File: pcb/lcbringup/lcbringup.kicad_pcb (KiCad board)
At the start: 4 copper layers, 198 parts, among them J1 XILINX_JTAG, J10 SMPM, J11 ARF6-08-S-D-A-K-TR, J12 SMPM, J13 SMPM, J14 SMPM, J15 SMPM, J16 SMPM, J17 SMPM, J18 SMPM, J19 SMPM, J2 CONN_01X10, J20 SMPM, J21 SMPM, J22 SMPM, J3 CONN_SFP_HOST, J4 CORTEX_DEBUG_ETM, J5 CONN_01X03, J6 CONN_01X03, J7 SFP_CAGE, J8 CONN_IBC_MGMT, J9 CONN_ATX12V, M1 SCREWHOLE, M2 SCREWHOLE, M3 SCREWHOLE, M4 SCREWHOLE, U1 XC7A35T-2FGG484C, U10 MUN12AD03-SE, U11 MUN12AD03-SE, U2 STM32H735-UFBGA176-25, U3 ECS-1612MV-250-CN, U4 ECS-1612MV-250-CN, U5 MUN12AD03-SE, U6 ECS-1612MV-250-CN, U7 AT24MAC402, U8 SIT9121AI-2BF-XXS156.250000G, U9 MUN12AD03-SE

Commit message: Continued lcbringup layout
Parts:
- removed D6, D7, D8, D9: GREEN, azonenberg_pcb:EIA_0402_LED
- removed J6: CONN_01X03, azonenberg_pcb:CONN_HEADER_2.54MM_1x3
- removed R12, R13, R14, R15: 33K, azonenberg_pcb:EIA_0402_RES_NOSILK
- removed R25: 33, azonenberg_pcb:EIA_0402_RES_NOSILK
- removed U6: ECS-1612MV-250-CN, azonenberg_pcb:OSCILLATOR_1.6x1.2
- added C92: 0.47 uF, azonenberg_pcb:EIA_0402_CAP_NOSILK, F.Cu at (92.5, 118.0)
- added J23: CONN_IBC_MGMT_HOST, azonenberg_pcb:CONN_MOLEX_PICOBLADE_5POS_0532610571, F.Cu at (62.8, 112.0)
- C14, C15, C17, C18, C19, C2, C21, C22, C23, C24, C25, C26, C27, C28, C29, C33, C34, C35, C36, C42, C44, C47, C48, C49, C51, C52, C54, C55, C56, C57, C58, C59, C69, C7, C70, C71, C78, C8, C9, R11, R2, R24, R3, R34, R4, U8: moved to B.Cu
- C61: value 0.47 uF -> 4.7 uF; footprint azonenberg_pcb:EIA_0402_CAP_NOSILK -> azonenberg_pcb:EIA_0603_CAP_NOSILK
- moved J10 137.6 mm to (12.6, 29.2)
- moved J11 137.6 mm to (32.6, 30.3)
- moved J12 137.6 mm to (18.1, 29.2)
- moved J13 137.6 mm to (23.6, 29.2)
- moved J14 137.6 mm to (12.6, 35.9)
- moved J15 137.6 mm to (18.1, 35.9)
- moved J16 137.6 mm to (23.6, 35.9)
- moved J17 137.6 mm to (12.6, 42.5)
- moved J18 137.6 mm to (18.1, 42.5)
- moved J19 137.6 mm to (23.6, 42.5)
- moved J20 137.6 mm to (12.6, 49.1)
- moved J21 137.6 mm to (18.1, 49.1)
- moved J22 137.6 mm to (23.6, 49.1)
- moved C72 110.5 mm to (-3.78, 69.4)
- moved C73 110.5 mm to (-3.78, 70.9)
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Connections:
- net /MCU/SUPER_I2C_SCL renamed /Power supply/SUPER_I2C_SCL
- net /MCU/SUPER_I2C_SDA renamed /Power supply/SUPER_I2C_SDA
- C70 pad 2: /SFP/GTP_REF_P -> /SFP/GTP_REF_N
- C71 pad 2: /SFP/GTP_REF_N -> /SFP/GTP_REF_P
- J3 pad 12: /SFP/SFP_RX_P -> /SFP/SFP_RX_N
- J3 pad 13: /SFP/SFP_RX_N -> /SFP/SFP_RX_P
- R24 pad 2: Net-(J6-P2) -> /GND
- U1 pad A18: unconnected-(U1F-IO_L17P_T2_16-PadA18) -> /MCU/FMC_AD8
- U1 pad A19: unconnected-(U1F-IO_L17N_T2_16-PadA19) -> /MCU/FMC_AD11
- U1 pad A20: unconnected-(U1F-IO_L16N_T2_16-PadA20) -> /MCU/FMC_AD15
- U1 pad A21: unconnected-(U1F-IO_L21N_T3_DQS_16-PadA21) -> /MCU/FMC_AD14
- U1 pad B18: unconnected-(U1F-IO_L11N_T1_SRCC_16-PadB18) -> /MCU/FMC_AD12
- U1 pad B20: unconnected-(U1F-IO_L16P_T2_16-PadB20) -> /MCU/FMC_AD13
- U1 pad B21: unconnected-(U1F-IO_L21P_T3_DQS_16-PadB21) -> /MCU/FMC_AD10
- U1 pad B22: unconnected-(U1F-IO_L20N_T3_16-PadB22) -> /MCU/FMC_A17
- U1 pad C22: unconnected-(U1F-IO_L20P_T3_16-PadC22) -> /MCU/FMC_A16
- U1 pad D21: unconnected-(U1F-IO_L23N_T3_16-PadD21) -> /MCU/FMC_A18
- U1 pad D22: unconnected-(U1F-IO_L22N_T3_16-PadD22) -> /MCU/FMC_AD0
- U1 pad E21: unconnected-(U1F-IO_L23P_T3_16-PadE21) -> /MCU/FMC_NE3
- U1 pad E22: unconnected-(U1F-IO_L22P_T3_16-PadE22) -> /MCU/FMC_NE1
- U1 pad G13: /MCU/FMC_AD13 -> unconnected-(U1E-IO_L1N_T0_AD0N_15-PadG13)
- U1 pad G15: /MCU/FMC_AD12 -> unconnected-(U1E-IO_L2P_T0_AD8P_15-PadG15)
- U1 pad G16: /MCU/FMC_AD10 -> unconnected-(U1E-IO_L2N_T0_AD8N_15-PadG16)
- U1 pad G18: /MCU/FMC_AD8 -> unconnected-(U1E-IO_L4N_T0_AD9N_15-PadG18)
- U1 pad G20: /MCU/FMC_NE1 -> /MCU/FMC_NWAIT
- U1 pad H13: /MCU/FMC_AD11 -> unconnected-(U1E-IO_L1P_T0_AD0P_15-PadH13)
- U1 pad H19: /MCU/FMC_AD15 -> /MCU/FMC_AD2
- U1 pad H20: /MCU/FMC_NWE -> /MCU/FMC_AD3
- U1 pad H22: /MCU/FMC_NE3 -> /MCU/FMC_NWE
- U1 pad J14: /MCU/FMC_AD9 -> /MCU/FMC_AD1
- U1 pad J16: /MCU/FMC_A18 -> unconnected-(U1E-IO_0_15-PadJ16)
- U1 pad J17: /MCU/FMC_A19 -> unconnected-(U1E-IO_L21N_T3_DQS_A18_15-PadJ17)
- U1 pad J20: /MCU/FMC_A24 -> /MCU/FMC_NOE
- U1 pad J21: /MCU/FMC_NL_NADV -> /MCU/FMC_NE2
- U1 pad J22: /MCU/FMC_AD0 -> /MCU/FMC_A25
- U1 pad K13: /MCU/FMC_A17 -> unconnected-(U1E-IO_L19P_T3_A22_15-PadK13)
- U1 pad K14: /MCU/FMC_AD14 -> unconnected-(U1E-IO_L19N_T3_A21_VREF_15-PadK14)
- U1 pad K16: /MCU/FMC_A21 -> unconnected-(U1E-IO_L23N_T3_FWE_B_15-PadK16)
- U1 pad K17: /MCU/FMC_NOE -> unconnected-(U1E-IO_L21P_T3_DQS_15-PadK17)
- U1 pad K18: /MCU/FPGA_CLK_25MHZ -> unconnected-(U1E-IO_L13P_T2_MRCC_15-PadK18)
- U1 pad K19: /MCU/FPGA_LED_0 -> /MCU/FMC_NBL1
- U1 pad K21: /MCU/FMC_AD2 -> /MCU/FMC_A24
- U1 pad K22: /MCU/FMC_NWAIT -> /MCU/FMC_NL_NADV
- U1 pad L13: /MCU/FMC_A23 -> unconnected-(U1E-IO_L20N_T3_A19_15-PadL13)
- U1 pad L15: /MCU/FMC_AD1 -> unconnected-(U1E-IO_L22N_T3_A16_15-PadL15)
- U1 pad L16: /MCU/FMC_A20 -> unconnected-(U1E-IO_L23P_T3_FOE_B_15-PadL16)
- U1 pad L18: /MCU/FMC_A22 -> unconnected-(U1E-IO_L16N_T2_A27_15-PadL18)
- U1 pad L19: /MCU/FPGA_LED_3 -> /MCU/FMC_A22
- U1 pad L20: unconnected-(U1E-IO_L14N_T2_SRCC_15-PadL20) -> /MCU/FMC_AD9
- U1 pad L21: /MCU/FMC_AD3 -> /MCU/FMC_NBL0
- U1 pad M13: /MCU/FMC_NBL0 -> unconnected-(U1E-IO_L20P_T3_A20_15-PadM13)
- U1 pad M17: /MCU/FPGA_LED_2 -> unconnected-(U1E-IO_25_15-PadM17)
- U1 pad M18: /MCU/FMC_A25 -> unconnected-(U1E-IO_L16P_T2_A28_15-PadM18)
- U1 pad M21: /MCU/FMC_NE2 -> /MCU/FMC_A23
- U1 pad M22: unconnected-(U1E-IO_L15N_T2_DQS_ADV_B_15-PadM22) -> /MCU/FMC_A19
- U1 pad N18: /MCU/FMC_NBL1 -> unconnected-(U1E-IO_L17P_T2_A26_15-PadN18)
- U1 pad N19: /MCU/FMC_A16 -> unconnected-(U1E-IO_L17N_T2_A25_15-PadN19)
- U1 pad N20: unconnected-(U1E-IO_L18P_T2_A24_15-PadN20) -> /MCU/FMC_A21
- U1 pad N22: /MCU/FPGA_LED_1 -> /MCU/FMC_A20
- U2 pad M1: unconnected-(U2C-PC2-PadM1) -> /MCU/MCU_LED_0
- U2 pad M2: unconnected-(U2C-PC3-PadM2) -> /MCU/MCU_LED_1
- U2 pad N11: /MCU/MCU_LED_1 -> unconnected-(U2F-PF13-PadN11)
- U2 pad N13: /MCU/MCU_LED_0 -> unconnected-(U2H-PH8-PadN13)
- U2 pad N7: /MCU/MCU_LED_3 -> unconnected-(U2F-PF11-PadN7)
- U2 pad P1: unconnected-(U2A-PA0-PadP1) -> /MCU/MCU_LED_2
- U2 pad P11: /MCU/MCU_LED_2 -> unconnected-(U2F-PF12-PadP11)
- U2 pad P2: unconnected-(U2A-PA1-PadP2) -> /MCU/MCU_LED_3
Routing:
- net /GND: track 0.00 -> 665.9 mm, vias 0 -> 179
- net /3V3: track 0.00 -> 252.0 mm, vias 0 -> 63
- net /SFP/SFP_I2C_SDA: track 0.00 -> 71.6 mm, vias 0 -> 6
- net /SFP/SFP_I2C_SCL: track 0.00 -> 66.2 mm, vias 0 -> 4
- net /1V0: track 0.00 -> 56.3 mm, vias 0 -> 22
- net /MCU/MCU_UART_RX: track 0.00 -> 36.9 mm, vias 0 -> 1
- net /MCU/FMC_AD9: track 0.00 -> 36.3 mm, vias 0 -> 4
- net /MCU/MCU_UART_TX: track 0.00 -> 36.1 mm, vias 0 -> 1
- net /MCU/FMC_AD8: track 0.00 -> 34.8 mm
- net /MCU/VSMPS: track 0.00 -> 31.6 mm, vias 0 -> 7
- net /MCU/FMC_AD12: track 0.00 -> 31.2 mm
- net /SFP/SFP_RX_P: track 0.00 -> 30.8 mm
- net /SFP/SFP_RX_N: track 0.00 -> 30.8 mm
- net /MCU/FMC_AD11: track 0.00 -> 29.9 mm
- net /MCU/FMC_AD6: track 0.00 -> 28.6 mm, vias 0 -> 1
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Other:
- board outline added: 80.8 x 80.5 mm
- board text added: "GND"
- board text added: "LED0"
- board text added: "LED1"
- board text added: "LED2"
- board text added: "LED3"
- board text added: "RX"
- board text added: "TX"
- board text added: "VDDA"

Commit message: Continued line card bringup board
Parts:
- C38, C62, C63, C67, C68, C92, R22, R23, R26, R27, R28, TP2, U7: moved to B.Cu
- C40: value 2.2 uF -> 4.7 uF; footprint azonenberg_pcb:EIA_0805_CAP_NOSILK -> azonenberg_pcb:EIA_0603_CAP_NOSILK; moved to B.Cu
- C44: value 2.2 uF -> 4.7 uF; footprint azonenberg_pcb:EIA_0805_CAP_NOSILK -> azonenberg_pcb:EIA_0603_CAP_NOSILK
- moved R28 103.0 mm to (97.0, 40.0)
- moved R23 102.2 mm to (97.0, 41.5)
- moved R22 80.6 mm to (79.0, 60.5), turned to -90 degrees
- moved TP2 68.1 mm to (111.0, 57.5), turned to 180 degrees
- moved C40 64.8 mm to (112.5, 61.0), turned to 90 degrees
- moved U7 57.3 mm to (124.5, 61.8)
- moved C63 57.0 mm to (85.0, 58.5), turned to -90 degrees
- moved C62 56.5 mm to (89.5, 57.0)
- moved C92 55.6 mm to (88.0, 62.5), turned to 90 degrees
- moved C67 55.3 mm to (86.0, 61.5), turned to -90 degrees
- moved C38 55.2 mm to (102.5, 68.8), turned to 180 degrees
- moved C68 51.8 mm to (123.0, 63.2), turned to 90 degrees
- moved TP1 50.3 mm to (120.0, 79.5)
- moved R27 49.5 mm to (125.8, 64.5), turned to -90 degrees
- moved J8 46.7 mm to (62.8, 123.5)
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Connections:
- U1 pad A16: unconnected-(U1F-IO_L9N_T1_DQS_16-PadA16) -> /MCU/FMC_AD4
- U1 pad AA21: unconnected-(U1D-IO_L8N_T1_D12_14-PadAA21) -> /MDIO and GPIO/ARTIX_LED_2
- U1 pad AB18: /MDIO and GPIO/ARTIX_LED_3 -> unconnected-(U1D-IO_L17N_T2_A13_D29_14-PadAB18)
- U1 pad AB20: /MDIO and GPIO/ARTIX_LED_2 -> /MDIO and GPIO/ARTIX_LED_3
- U1 pad B16: unconnected-(U1F-IO_L7N_T1_16-PadB16) -> /MCU/FMC_AD7
- U1 pad B17: unconnected-(U1F-IO_L11P_T1_SRCC_16-PadB17) -> /MCU/FMC_AD6
- U1 pad D16: unconnected-(U1F-IO_L5N_T0_16-PadD16) -> /MCU/FMC_AD5
- U1 pad E16: unconnected-(U1F-IO_L5P_T0_16-PadE16) -> /MCU/FMC_AD1
- U1 pad G17: /MCU/FMC_AD6 -> unconnected-(U1E-IO_L4P_T0_AD9P_15-PadG17)
- U1 pad H14: /MCU/FMC_AD5 -> unconnected-(U1E-IO_L3N_T0_DQS_AD1N_15-PadH14)
- U1 pad H15: /MCU/FMC_AD4 -> unconnected-(U1E-IO_L5N_T0_AD9N_15-PadH15)
- U1 pad H18: /MCU/FMC_AD7 -> unconnected-(U1E-IO_L6N_T0_VREF_15-PadH18)
- U1 pad J14: /MCU/FMC_AD1 -> unconnected-(U1E-IO_L3P_T0_DQS_AD1P_15-PadJ14)
- U1 pad N14: /MDIO and GPIO/MDC -> unconnected-(U1D-IO_L23N_T3_A02_D18_14-PadN14)
- U1 pad N17: /MDIO and GPIO/SPI_MOSI -> unconnected-(U1D-IO_L21P_T3_DQS_14-PadN17)
- U1 pad P16: /MDIO and GPIO/MDIO -> unconnected-(U1D-IO_L24P_T3_A01_D17_14-PadP16)
- U1 pad R14: /MDIO and GPIO/SPI_CS_N -> unconnected-(U1D-IO_L19N_T3_A09_D25_VREF_14-PadR14)
- U1 pad R18: /MDIO and GPIO/SPI_SCK -> unconnected-(U1D-IO_L20P_T3_A08_D24_14-PadR18)
- U1 pad R22: unconnected-(U1D-IO_L1N_T0_D01_DIN_14-PadR22) -> /MDIO and GPIO/SPI_CS_N
- U1 pad T18: /MDIO and GPIO/SPI_MISO -> unconnected-(U1D-IO_L20N_T3_A07_D23_14-PadT18)
- U1 pad V22: unconnected-(U1D-IO_L3N_T0_DQS_EMCCLK_14-PadV22) -> /MDIO and GPIO/SPI_MISO
- U1 pad W21: unconnected-(U1D-IO_L7P_T1_D09_14-PadW21) -> /MDIO and GPIO/MDC
- U1 pad W22: unconnected-(U1D-IO_L7N_T1_D10_14-PadW22) -> /MDIO and GPIO/SPI_SCK
- U1 pad Y21: unconnected-(U1D-IO_L9P_T1_DQS_14-PadY21) -> /MDIO and GPIO/MDIO
- U1 pad Y22: unconnected-(U1D-IO_L9N_T1_DQS_D13_14-PadY22) -> /MDIO and GPIO/SPI_MOSI
- U2 pad C12: unconnected-(U2C-PC10-PadC12) -> /MCU/SFP_RS1
- U2 pad C13: /MCU/SFP_TX_FAULT -> unconnected-(U2H-PH13-PadC13)
- U2 pad D12: /MCU/SFP_RS1 -> unconnected-(U2H-PH15-PadD12)
- U2 pad M13: /MCU/SFP_TX_DISABLE -> unconnected-(U2H-PH11-PadM13)
- U2 pad N14: /MCU/SFP_RX_LOS -> unconnected-(U2H-PH10-PadN14)
- U2 pad N15: /MCU/SFP_MOD_ABS -> unconnected-(U2H-PH12-PadN15)
- U2 pad P7: unconnected-(U2B-PB2-PadP7) -> /MCU/SFP_TX_FAULT
- U2 pad P8: unconnected-(U2G-PG0-PadP8) -> /MCU/SFP_RX_LOS
- U2 pad R7: unconnected-(U2A-PA6-PadR7) -> /MCU/SFP_MOD_ABS
- U2 pad R8: unconnected-(U2B-PB0-PadR8) -> /MCU/SFP_TX_DISABLE
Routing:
- net /GND: track 665.9 -> 733.9 mm, vias 179 -> 192
- net /3V3: track 252.0 -> 317.7 mm, vias 63 -> 70
- net /Power supply/SUPER_I2C_SDA: track 0.00 -> 60.1 mm, vias 0 -> 2
- net /MDIO and GPIO/SPI_MOSI: track 0.00 -> 57.0 mm, vias 0 -> 2
- net /MDIO and GPIO/SPI_MISO: track 0.00 -> 54.0 mm, vias 0 -> 2
- net /MDIO and GPIO/SPI_CS_N: track 0.00 -> 53.4 mm, vias 0 -> 2
- net /MDIO and GPIO/SPI_SCK: track 0.00 -> 52.9 mm, vias 0 -> 2
- net /MDIO and GPIO/MDIO: track 0.00 -> 52.3 mm, vias 0 -> 2
- net /MDIO and GPIO/MDC: track 0.00 -> 51.3 mm, vias 0 -> 2
- net /Power supply/SUPER_I2C_SCL: track 9.53 -> 59.7 mm, vias 1 -> 2
- net /MCU/FMC_AD1: track 0.00 -> 39.1 mm, vias 0 -> 4
- net /MCU/SFP_MOD_ABS: track 0.00 -> 38.3 mm, vias 0 -> 2
- net /MCU/SFP_RX_LOS: track 0.00 -> 37.6 mm
- net /MCU/SFP_TX_FAULT: track 0.00 -> 37.1 mm, vias 0 -> 2
- net /MCU/SFP_TX_DISABLE: track 0.00 -> 31.6 mm
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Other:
- board size 80.8 x 80.5 mm -> 80.8 x 69 mm
- board text added: "SCL"
- board text added: "SDA"
- board text added: "VCORE"

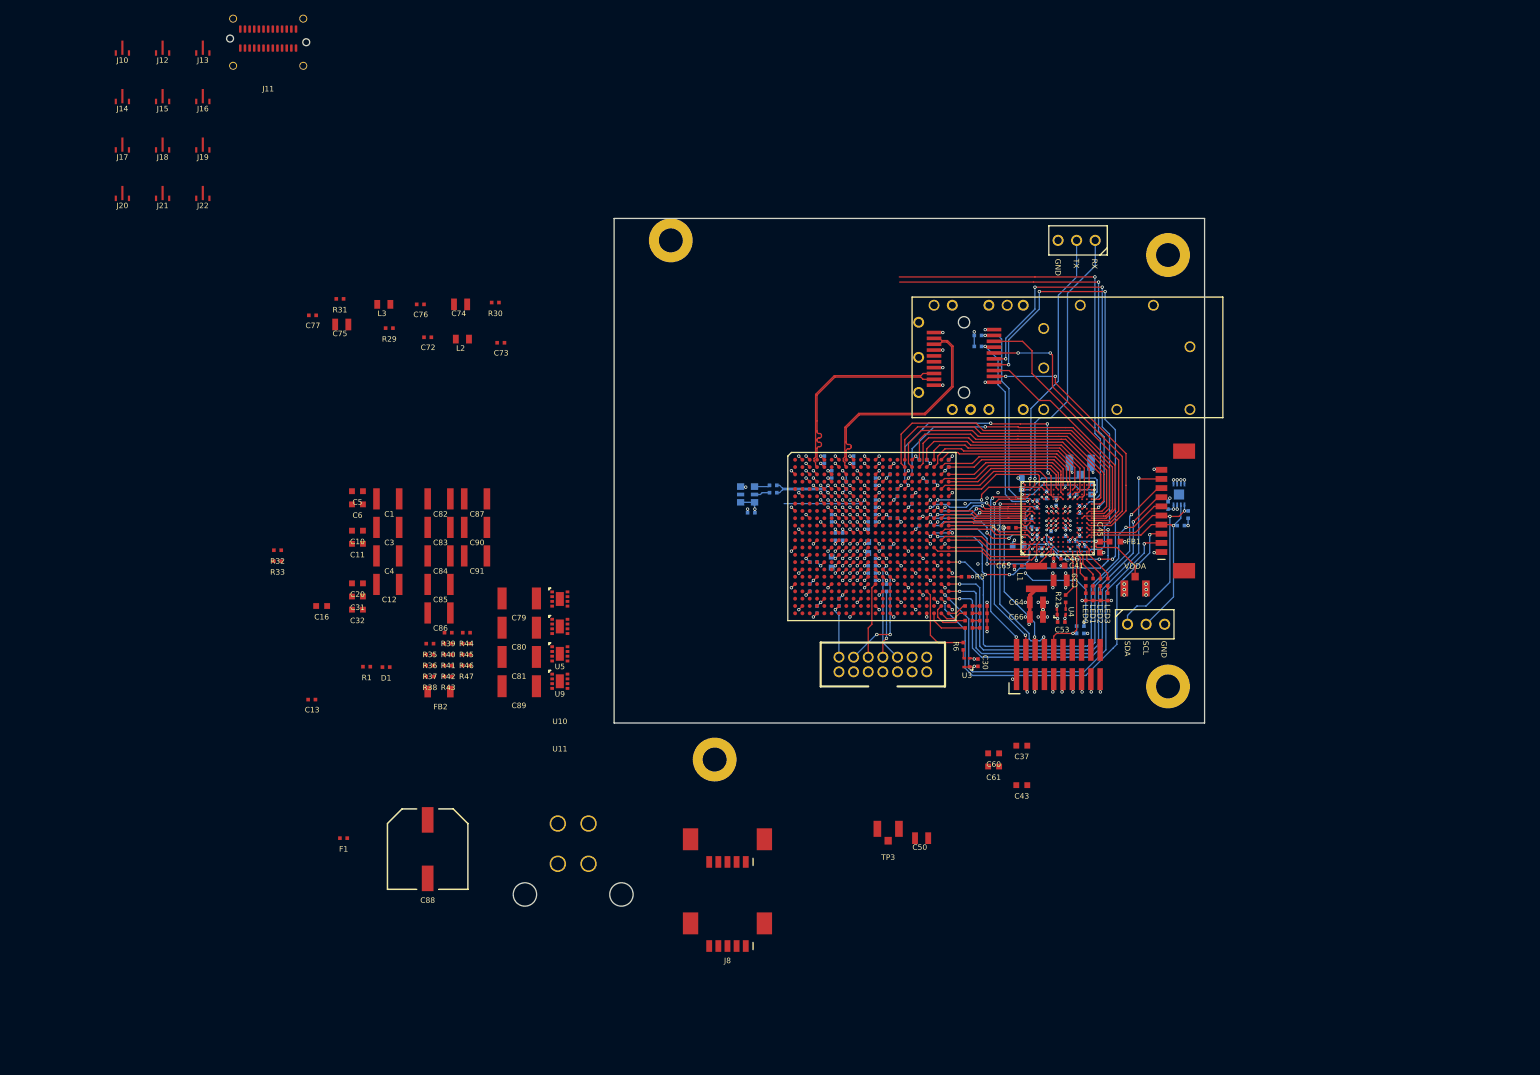
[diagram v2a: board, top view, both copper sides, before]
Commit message: Initial directory structure for line card firmware
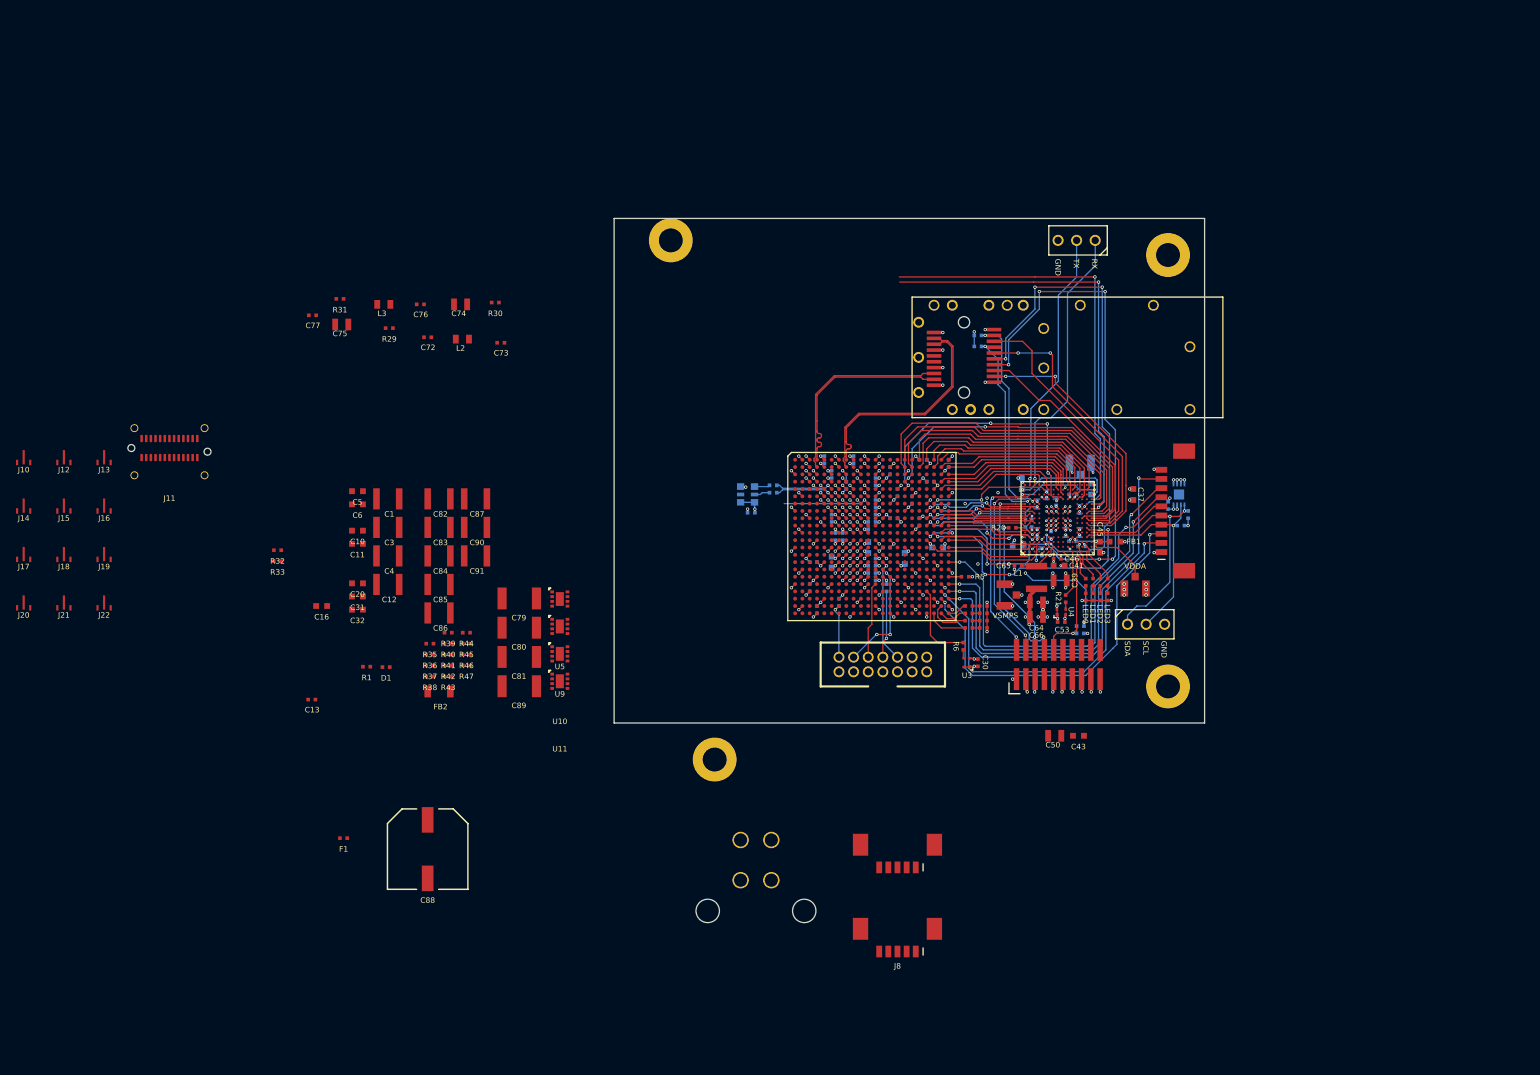
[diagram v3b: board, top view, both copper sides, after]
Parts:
- C60, C61: moved to B.Cu
- moved J10 57.6 mm to (-33.5, 54.4)
- moved J11 57.6 mm to (-13.6, 55.4)
- moved J12 57.6 mm to (-28.0, 54.4)
- moved J13 57.6 mm to (-22.5, 54.4)
- moved J14 57.6 mm to (-33.5, 61.0)
- moved J15 57.6 mm to (-28.0, 61.0)
- moved J16 57.6 mm to (-22.5, 61.0)
- moved J17 57.6 mm to (-33.5, 67.6)
- moved J18 57.6 mm to (-28.0, 67.6)
- moved J19 57.6 mm to (-22.5, 67.6)
- moved J20 57.6 mm to (-33.5, 74.2)
- moved J21 57.6 mm to (-28.0, 74.2)
- moved J22 57.6 mm to (-22.5, 74.2)
- moved C37 37.6 mm to (118.2, 61.8), turned to -90 degrees
- moved TP3 35.9 mm to (100.8, 75.5), turned to 90 degrees
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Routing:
- net /GND: track 733.9 -> 745.1 mm, vias 192 -> 195
- net /3V3: track 317.7 -> 326.1 mm, vias 70 -> 71
- net /MCU/VSMPS: track 42.2 -> 43.4 mm, vias 7 -> 8
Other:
- board text added: "VSMPS"
